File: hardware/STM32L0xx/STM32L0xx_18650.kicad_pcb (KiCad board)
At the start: 2 copper layers, 109.7 x 16 mm, 54 parts, among them J2 Battery, J3 GPIO, J4 USB_B_Micro, J5 Power, J6 LEDs, J7 GPIO, Q1 BSS806N, Q2 BSS806N, Q3 BSS806N, Q4 BSS806N, SW1 Mode, SW2 Power, U1 STM32L072KZTx, U2 AP2210N-3.3TRG1, U3 BQ21040, U4 ESD7002WTT1G, Y1 32.768kHz

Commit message: Change `PWM` to `LEDs`
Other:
- board text added: "LEDs"
- board text removed: "PWM"
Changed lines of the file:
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@@
     (effects (font (size 0.65 0.65) (thickness 0.1)) (justify mirror))
   )
-  (gr_text PWM (at 115.65 93.525) (layer B.SilkS)
+  (gr_text LEDs (at 115.65 93.525) (layer B.SilkS)
     (effects (font (size 1 1) (thickness 0.2)) (justify mirror))
   )

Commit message: Update hardware silkscreens
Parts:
- moved REF** 0.72 mm to (146.6, 99.9)
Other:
- board text added: "Created by Jeremy Gillick https://github.com/jgillick/ThunderPack"
- board text added: "Vin"
- board text added: "rev 1"
- board text removed: "Created by Jeremy Gillick"
- board text removed: "rev 1a5"
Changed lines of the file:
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@@
   )
   (setup
-    (last_trace_width 0.762)
+    (last_trace_width 0.1524)
     (user_trace_width 0.254)
     (user_trace_width 0.31)
@@
   )
   (module Symbol:OSHW-Logo2_9.8x8mm_Copper (layer B.Cu)
-    (at 145.925 100.2 180)
+    (at 146.575 99.9 180)
     (descr "Open Source Hardware Symbol")
     (tags "Logo Symbol OSHW")
@@
       (net 18 /PA8))
   )
-  (gr_text CLK (at 87.35 107.425) (layer B.Mask)
+  (gr_text CLK (at 87.35 107.425) (layer B.SilkS)
     (effects (font (size 0.6 0.6) (thickness 0.1)) (justify mirror))
   )
-  (gr_text DIO (at 84.65 107.425) (layer B.Mask)
+  (gr_text DIO (at 84.65 107.425) (layer B.SilkS)
     (effects (font (size 0.6 0.6) (thickness 0.1)) (justify mirror))
   )
@@
     (effects (font (size 1 1) (thickness 0.2)))
   )
-  (gr_text "rev 1a5" (at 153.5 96.525) (layer B.SilkS)
+  (gr_text "rev 1" (at 153.5 96.525) (layer B.SilkS)
     (effects (font (size 0.8 0.8) (thickness 0.1)) (justify left mirror))
   )
@@
     (effects (font (size 0.65 0.65) (thickness 0.1)))
   )
-  (gr_text "Created by Jeremy Gillick" (at 153.9 105.375) (layer B.SilkS)
+  (gr_text "Created by Jeremy Gillick\nhttps://github.com/jgillick/ThunderPack" (at 153.7 105.35) (layer B.SilkS)
     (effects (font (size 0.8 0.8) (thickness 0.1)) (justify left mirror))
   )
@@
     (effects (font (size 1 1) (thickness 0.2)) (justify mirror))
   )
-  (gr_text Batt+ (at 120.55 103.9) (layer B.SilkS)
+  (gr_text Vin (at 120.35 103.9) (layer B.SilkS)
     (effects (font (size 0.65 0.65) (thickness 0.1)) (justify mirror))
   )
@@
   (segment (start 81.042599 93.232401) (end 81.875 92.4) (width 0.31) (layer B.Cu) (net 4))
   (via (at 82.75 97.675) (size 0.508) (drill 0.254) (layers F.Cu B.Cu) (net 4))
-  (segment (start 82.425 99.375) (end 81.7426 99.375) (width 0.1524) (layer F.Cu) (net 35))
-  (segment (start 81.7426 99.375) (end 81.188999 98.821399) (width 0.1524) (layer F.Cu) (net 35))
   (via (at 134.35 97.125) (size 0.508) (drill 0.254) (layers F.Cu B.Cu) (net 5))
   (segment (start 139.15 101.925) (end 139.15 102.675) (width 0.31) (layer B.Cu) (net 5) (status 30))
@@
   (segment (start 80.0625 101.4375) (end 80.225 101.275) (width 0.31) (layer F.Cu) (net 6))
   (segment (start 78.625 101.4375) (end 80.0625 101.4375) (width 0.31) (layer F.Cu) (net 6))
-  (segment (start 126.35 92.4) (end 134.175 92.4) (width 0.31) (layer F.Cu) (net 6) (status 1000000))
-  (segment (start 134.175 92.4) (end 139.15 97.375) (width 0.31) (layer F.Cu) (net 6) (status 1000020))
-  (segment (start 125.5 93.25) (end 126.35 92.4) (width 0.31) (layer F.Cu) (net 6) (status 1000010))
+  (segment (start 126.35 92.4) (end 134.175 92.4) (width 0.31) (layer F.Cu) (net 6))
+  (segment (start 134.175 92.4) (end 139.15 97.375) (width 0.31) (layer F.Cu) (net 6) (status 20))
+  (segment (start 125.5 93.25) (end 126.35 92.4) (width 0.31) (layer F.Cu) (net 6) (status 10))
   (segment (start 130.6875 93.35) (end 130.7125 93.375) (width 0.31) (layer F.Cu) (net 7) (status 30))
   (segment (start 128.9875 93.35) (end 130.6875 93.35) (width 0.31) (layer F.Cu) (net 7) (status 30))
@@
   (segment (start 83.9375 102.55) (end 82.342078 102.55) (width 0.254) (layer F.Cu) (net 34))
   (segment (start 82.342078 102.55) (end 81.034401 101.242323) (width 0.254) (layer F.Cu) (net 34))
+  (segment (start 82.425 99.375) (end 81.7426 99.375) (width 0.1524) (layer F.Cu) (net 35))
+  (segment (start 81.7426 99.375) (end 81.188999 98.821399) (width 0.1524) (layer F.Cu) (net 35))
   (segment (start 63.725 93.475) (end 63.1875 93.475) (width 0.1524) (layer F.Cu) (net 35))
   (segment (start 73.62533 93.475) (end 63.725 93.475) (width 0.1524) (layer F.Cu) (net 35))
+  (segment (start 78.971729 98.821399) (end 73.62533 93.475) (width 0.1524) (layer F.Cu) (net 35))
+  (segment (start 81.188999 98.821399) (end 78.971729 98.821399) (width 0.1524) (layer F.Cu) (net 35))
   (segment (start 105.7 98.7875) (end 104.2 98.7875) (width 0.1524) (layer F.Cu) (net 36) (status 30))
   (segment (start 104.2 98.7875) (end 102.7 98.7875) (width 0.1524) (layer F.Cu) (net 36) (status 30))
@@
   (segment (start 96.27139 103.80361) (end 91.64639 103.80361) (width 0.1524) (layer F.Cu) (net 40))
   (segment (start 83.7375 101.275) (end 83.9375 101.075) (width 0.254) (layer F.Cu) (net 41))
-  (segment (start 78.971729 98.821399) (end 73.62533 93.475) (width 0.1524) (layer F.Cu) (net 35))
-  (segment (start 81.188999 98.821399) (end 78.971729 98.821399) (width 0.1524) (layer F.Cu) (net 35))
   (segment (start 82.425 101.275) (end 83.7375 101.275) (width 0.254) (layer F.Cu) (net 41))
   (segment (start 92.675 100.6) (end 92.625 100.65) (width 0.1524) (layer F.Cu) (net 42) (status 30))
@@
       )
     )
-  )
-  (zone (net 0) (net_name "") (layer B.SilkS) (hatch full 0.508)
-    (connect_pads (clearance 0.381))
-    (min_thickness 0.254)
-    (fill yes (arc_segments 32) (thermal_gap 0.508) (thermal_bridge_width 0.508))
-    (polygon
-      (pts
-        (xy 88.3875 106.85625) (xy 88.4125 107.90625) (xy 86.3875 107.89375) (xy 86.3625 106.84375)
-      )
-    )
-  )
-  (zone (net 0) (net_name "") (layer B.SilkS) (hatch edge 0.508)
-    (connect_pads (clearance 0.381))
-    (min_thickness 0.254)
-    (fill yes (arc_segments 32) (thermal_gap 0.508) (thermal_bridge_width 0.508))
-    (polygon
-      (pts
-        (xy 85.525 106.85) (xy 85.525 107.9) (xy 83.775 107.9) (xy 83.775 106.85)
-      )
-    )

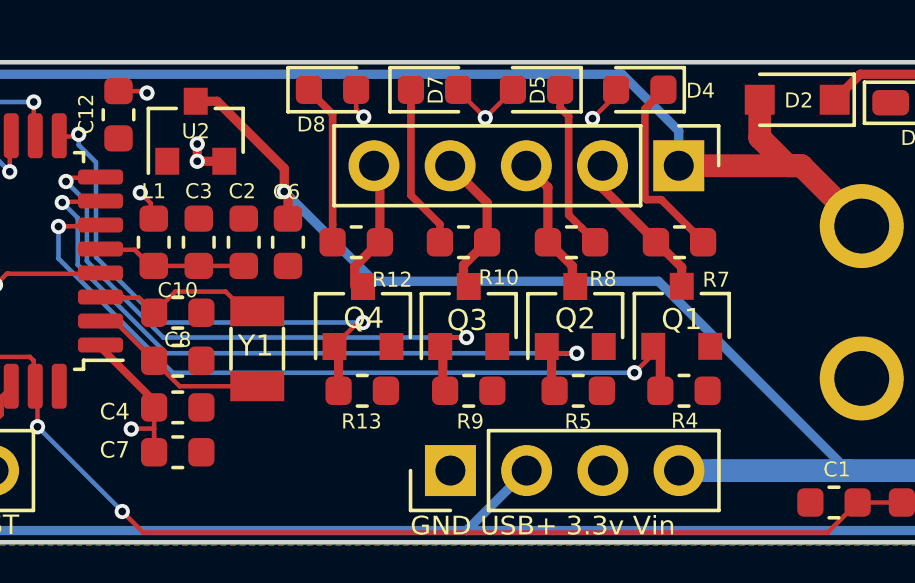
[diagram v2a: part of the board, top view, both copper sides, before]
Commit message: Adjust resistors.
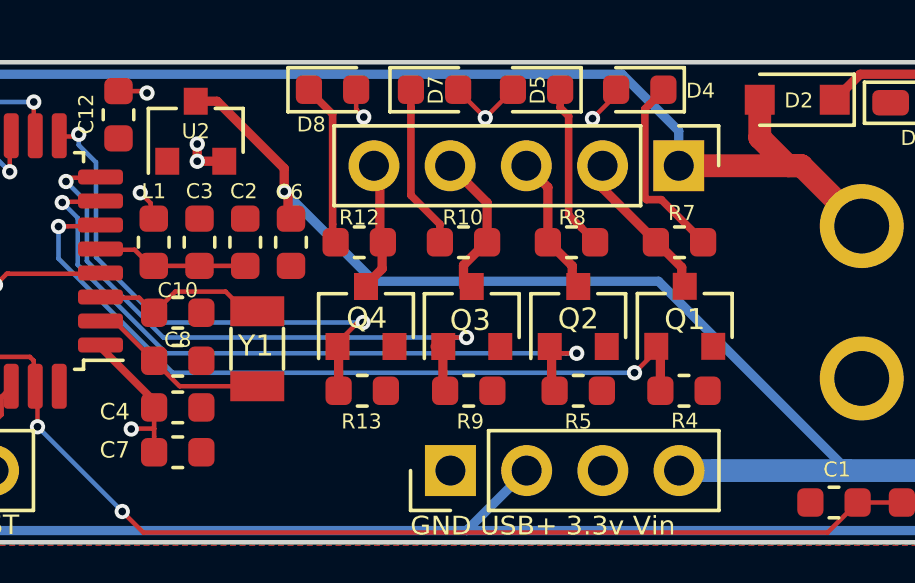
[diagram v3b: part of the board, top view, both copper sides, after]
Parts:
- moved Q2 0.10 mm to (117.0, 100.5)
- moved Q3 0.10 mm to (113.4, 100.5)
- moved R12 0.10 mm to (109.7, 98.0)
- moved C6 0.10 mm to (107.4, 98.0)
- moved Q1 0.10 mm to (120.5, 100.5)
- moved Q4 0.10 mm to (109.9, 100.5)
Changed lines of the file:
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@@
-(kicad_pcb (version 20171130) (host pcbnew "(5.1.4-0-10_14)")
+(kicad_pcb (version 20171130) (host pcbnew "(5.1.5-0-10_14)")
   (general
     (thickness 1.6)
@@
   )
   (setup
-    (last_trace_width 0.1524)
+    (last_trace_width 0.31)
     (user_trace_width 0.254)
     (user_trace_width 0.31)
@@
   )
   (module Capacitor_SMD:C_0603_1608Metric (layer F.Cu)
-    (at 107.275 98 270)
+    (at 107.375 98 270)
     (descr "Capacitor SMD 0603 (1608 Metric), square (rectangular) end terminal, IPC_7351 nominal, (Body size source: http://www.tortai-tech.com/upload/download/2011102023233369053.pdf), generated with kicad-footprint-generator")
     (tags capacitor)
@@
     (tags resistor)
     (attr smd)
-    (fp_text reference R7 (at -1.225 -1.25) (layer F.SilkS)
+    (fp_text reference R7 (at -0.075 0.975) (layer F.SilkS)
       (effects (font (size 0.5 0.5) (thickness 0.1)))
     )
@@
     (tags resistor)
     (attr smd)
-    (fp_text reference R8 (at -1.05 -1.225) (layer F.SilkS)
+    (fp_text reference R8 (at -0.025 0.825) (layer F.SilkS)
       (effects (font (size 0.5 0.5) (thickness 0.1)))
     )
@@
     (tags resistor)
     (attr smd)
-    (fp_text reference R10 (at 1.175 1.175) (layer F.SilkS)
+    (fp_text reference R10 (at -0.025 -0.825) (layer F.SilkS)
       (effects (font (size 0.5 0.5) (thickness 0.1)))
     )
@@
   )
   (module Resistor_SMD:R_0603_1608Metric (layer F.Cu)
-    (at 109.55 98)
+    (at 109.65 98)
     (descr "Resistor SMD 0603 (1608 Metric), square (rectangular) end terminal, IPC_7351 nominal, (Body size source: http://www.tortai-tech.com/upload/download/2011102023233369053.pdf), generated with kicad-footprint-generator")
     (tags resistor)
     (attr smd)
-    (fp_text reference R12 (at 1.2 1.25 180) (layer F.SilkS)
+    (fp_text reference R12 (at 0 -0.825 180) (layer F.SilkS)
       (effects (font (size 0.5 0.5) (thickness 0.1)))
     )
@@
   )
   (module Capacitor_SMD:C_0603_1608Metric (layer F.Cu)
-    (at 105.8 98 90)
+    (at 105.85 98 90)
     (descr "Capacitor SMD 0603 (1608 Metric), square (rectangular) end terminal, IPC_7351 nominal, (Body size source: http://www.tortai-tech.com/upload/download/2011102023233369053.pdf), generated with kicad-footprint-generator")
     (tags capacitor)
@@
   )
   (module Capacitor_SMD:C_0603_1608Metric (layer F.Cu)
-    (at 104.3 98 90)
+    (at 104.325 98 90)
     (descr "Capacitor SMD 0603 (1608 Metric), square (rectangular) end terminal, IPC_7351 nominal, (Body size source: http://www.tortai-tech.com/upload/download/2011102023233369053.pdf), generated with kicad-footprint-generator")
     (tags capacitor)
@@
   )
   (module Package_TO_SOT_SMD:SOT-23 (layer F.Cu)
-    (at 120.4 100.47 90)
+    (at 120.5 100.47 90)
     (descr "SOT-23, Standard")
     (tags SOT-23)
@@
   )
   (module Package_TO_SOT_SMD:SOT-23 (layer F.Cu)
-    (at 113.3 100.475 90)
+    (at 113.4 100.475 90)
     (descr "SOT-23, Standard")
     (tags SOT-23)
@@
   )
   (module Package_TO_SOT_SMD:SOT-23 (layer F.Cu)
-    (at 109.775 100.475 90)
+    (at 109.875 100.475 90)
     (descr "SOT-23, Standard")
     (tags SOT-23)
@@
   )
   (module Package_TO_SOT_SMD:SOT-23 (layer F.Cu)
-    (at 116.85 100.475 90)
+    (at 116.95 100.475 90)
     (descr "SOT-23, Standard")
     (tags SOT-23)
@@
   (segment (start 113.9125 96.6825) (end 112.68 95.45) (width 0.31) (layer F.Cu) (net 27) (status 20))
   (segment (start 113.9125 97.975) (end 113.9125 96.6825) (width 0.31) (layer F.Cu) (net 27) (status 10))
-  (segment (start 109.5 98.8125) (end 110.3375 97.975) (width 0.31) (layer F.Cu) (net 28) (status 20))
-  (segment (start 109.5 99.475) (end 109.5 98.8125) (width 0.31) (layer F.Cu) (net 28) (status 10))
   (segment (start 110.3375 95.6475) (end 110.14 95.45) (width 0.31) (layer F.Cu) (net 28) (status 30))
   (segment (start 110.3375 97.975) (end 110.3375 95.6475) (width 0.31) (layer F.Cu) (net 28) (status 30))
+  (segment (start 110.4125 98.8875) (end 109.825 99.475) (width 0.31) (layer F.Cu) (net 28))
+  (segment (start 110.4125 98) (end 110.4125 98.8875) (width 0.31) (layer F.Cu) (net 28))
   (segment (start 119.6875 101.7375) (end 119.45 101.5) (width 0.31) (layer F.Cu) (net 29) (status 30))
   (segment (start 119.6875 103) (end 119.6875 101.7375) (width 0.31) (layer F.Cu) (net 29) (status 30))
